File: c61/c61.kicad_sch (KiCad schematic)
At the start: 15 parts, among them J1 Conn_01x14, U1 ESP32-C61HF4, U2 TPS63900DSKR, Y1 Crystal

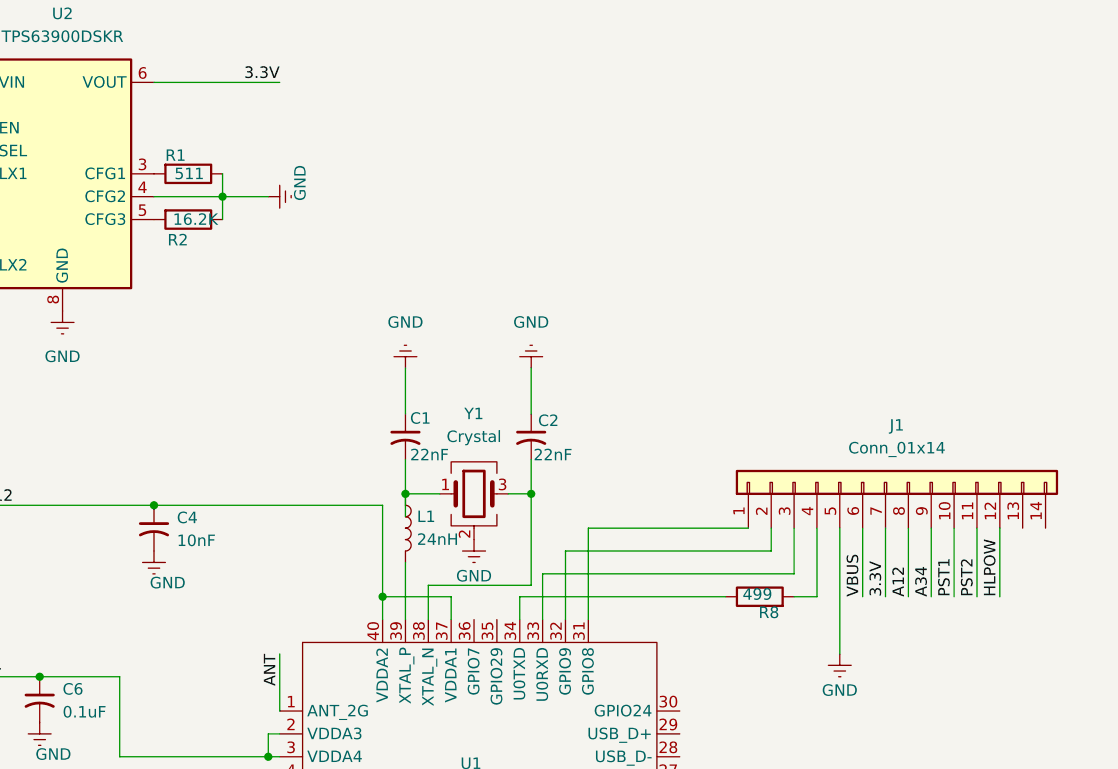
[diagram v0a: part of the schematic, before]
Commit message: c61 bare done
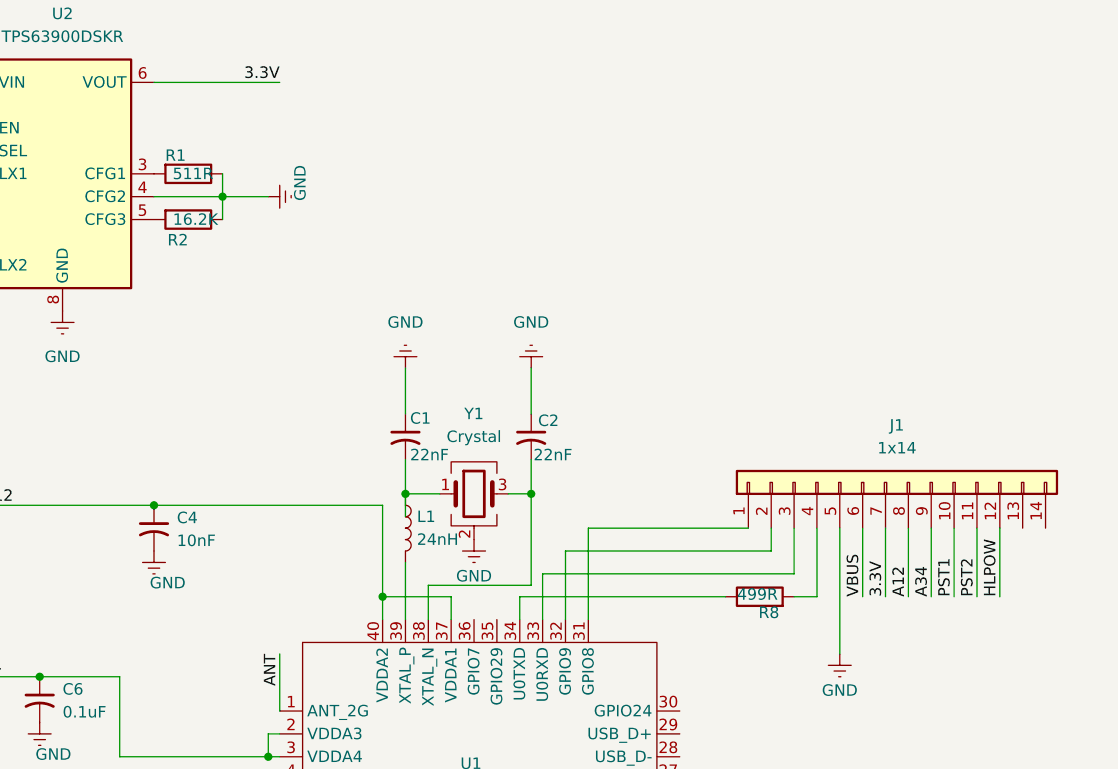
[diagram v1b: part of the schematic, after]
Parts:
- J1: value Conn_01x14 -> 1x14
- R1: value 511 -> 511R
- R8: value 499 -> 499R
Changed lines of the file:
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@@
 			)
 		)
-		(property "Value" "511"
-			(at 104.648 43.18 90)
+		(property "Value" "511R"
+			(at 105.664 43.18 90)
 			(show_name no)
 			(do_not_autoplace no)
@@
 			)
 		)
-		(property "Value" "Conn_01x14"
+		(property "Value" "1x14"
 			(at 181.61 73.66 90)
 			(show_name no)
@@
 			)
 		)
-		(property "Value" "499"
+		(property "Value" "499R"
 			(at 166.116 89.916 90)
 			(show_name no)

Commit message: no epaper this time
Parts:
- Y1: value Crystal -> Crystal 40MHz
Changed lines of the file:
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@@
 			)
 		)
-		(property "Value" "Crystal"
+		(property "Value" "Crystal 40MHz"
 			(at 134.62 72.39 0)
 			(show_name no)
